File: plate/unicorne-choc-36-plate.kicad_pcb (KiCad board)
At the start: 2 copper layers, 260.3 x 113.7 mm, 10 parts

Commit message: Cut the 36-key plates evenly on both sides
The Choc PCB's break lines sit 8.4 / 10.6 mm from the outer key column because
its sockets aren't mirrored; the plate now uses their average on both sides,
so both 36-key plates are symmetric.

Co-Authored-By: Claude Opus 5.5 <noreply@anthropic.com>
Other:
- board size 260.3 x 113.7 mm -> 260.3 x 113.5 mm

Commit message: Halves closer, trackpad on the case; GND repair in the router; re-export
- The trackpad sits on the case above the board, so it may cover the
  nice!nano. layout.py places it where its keycap keep-out lets the halves
  come closest: each half moves 3.25 mm inward and the board is 293.4 mm wide
  (was 299.9). The parts below it follow; it has no 3D model on the board.
- The level shifter group (U2, C2, JP3) moves down, clear of the inner
  column, which now comes within ~6.5 mm of the headers.
- J3/J4 headers have no 3D model (bare holes in the renders and STEP).
- finish_route.py: jitters the routing order between attempts, and repairs
  GND the pours left cut off (tools/gnd_repair.py: a via where the pocket
  overlaps the main ground, else rip up the net boxing it in and reroute).
- Both boards rerouted: DRC 0 unconnected, schematic parity 0, every pin,
  the matrix, the LED chain and one GND group verified. Gerbers, STEP,
  renders and all four plates regenerated. copper_sliver (a thin point in a
  GND pour) counts as harmless for the gerber export.

Co-Authored-By: Claude Opus 5.5 <noreply@anthropic.com>
Claude-Session: https://claude.ai/code/session_01D39ubfTYtq6FMvNmmbStTo
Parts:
- moved H5 6.25 mm to (217.7, 73.6)
- moved H6 6.25 mm to (257.0, 100.0)
- moved H7 6.25 mm to (219.3, 121.6)
- moved H8 6.25 mm to (276.8, 59.1)
- moved H10 3.59 mm to (191.0, 131.6)
- moved H9 3.59 mm to (163.0, 131.6)
- moved H1 0.25 mm to (133.3, 70.3)
- moved H2 0.25 mm to (97.0, 100.0)
- moved H3 0.25 mm to (135.2, 121.6)
- moved H4 0.25 mm to (76.7, 58.8)
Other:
- board size 260.3 x 113.5 mm -> 253.8 x 113.5 mm

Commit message: Plates: openings for the nice!nano (through the top edge) and the reset switch
Both from where the PCB has them, 0.5 mm clearance, 0.8 mm corner radius. The
nano opening joins the trackpad opening; all four plates pass DRC.

Co-Authored-By: Claude Opus 5.5 <noreply@anthropic.com>
Claude-Session: https://claude.ai/code/session_01D39ubfTYtq6FMvNmmbStTo
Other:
- outline, holes or cut-outs redrawn

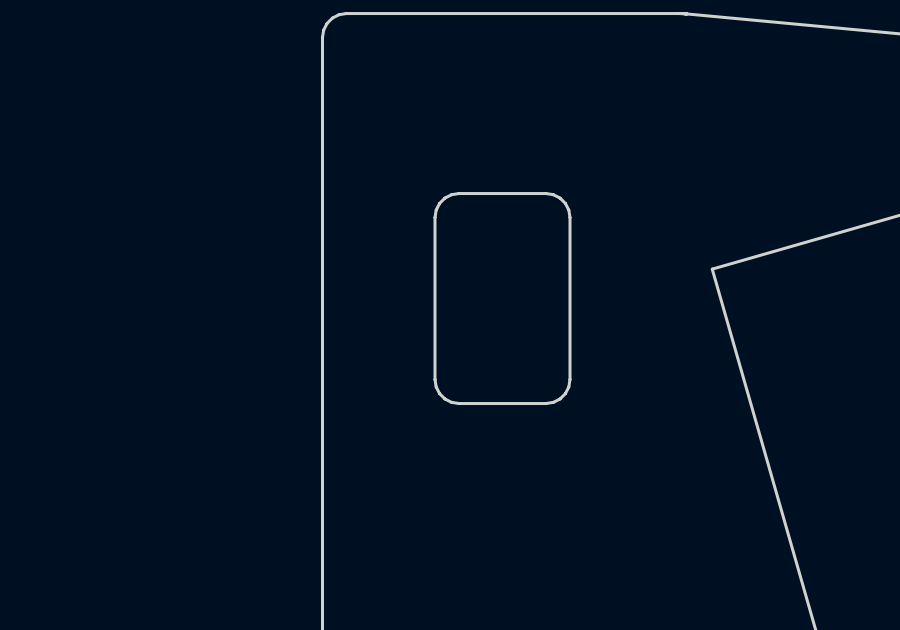
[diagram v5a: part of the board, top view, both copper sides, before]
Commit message: Route both boards with KiCadRoutingTools; no vias in pads
tools/krt_route.py: fixed lanes, then KiCadRoutingTools 0.23.7 for every other
signal at standard JLCPCB sizes (0.6/0.3 vias, 0.2 tracks) with no via in or next
to a pad, own net's included; the maze router for any net it could only finish
with undersized vias; GND pours and stitching; its plane repair; then any via
touching a pad is removed. The tools relax the project's rules on disk: ours are
put back.

MX lanes: LED_VDD's jog across a break line moves from 5.5 to 4.5 mm off the
line. At 5.5 it boxed in the outer-column LED DIN pads, so 8 LED data links had
no room for a via outside a pad. Lane-only board: no DRC errors.

Stitching vias (finish_route.stitch) and our maze router stay off SMD pads too.
The previous MX board had 82 vias in pads, now none on either board.

MX: U2 pad 3 (GND) is boxed in by LED_DIN; joined by hand with a via between
pads 3 and 4 (noted in the README).

Both boards: DRC 0 unconnected, 0 copper violations, schematic parity clean;
all 482 schematic pins, 42 keys and the 54-LED chain check out pin by pin.
Waves, LED map, plates, gerbers, STEP and renders regenerated.

Co-Authored-By: Claude Opus 5.5 <noreply@anthropic.com>
Claude-Session: https://claude.ai/code/session_01D39ubfTYtq6FMvNmmbStTo
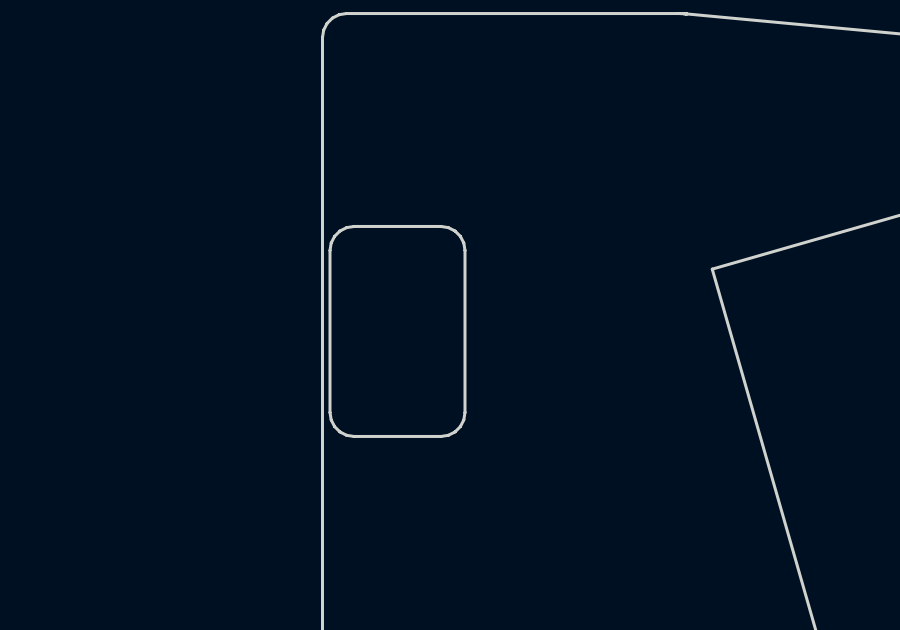
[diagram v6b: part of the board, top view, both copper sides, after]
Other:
- outline, holes or cut-outs redrawn
